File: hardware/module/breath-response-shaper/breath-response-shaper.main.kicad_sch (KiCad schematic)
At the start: 12 parts

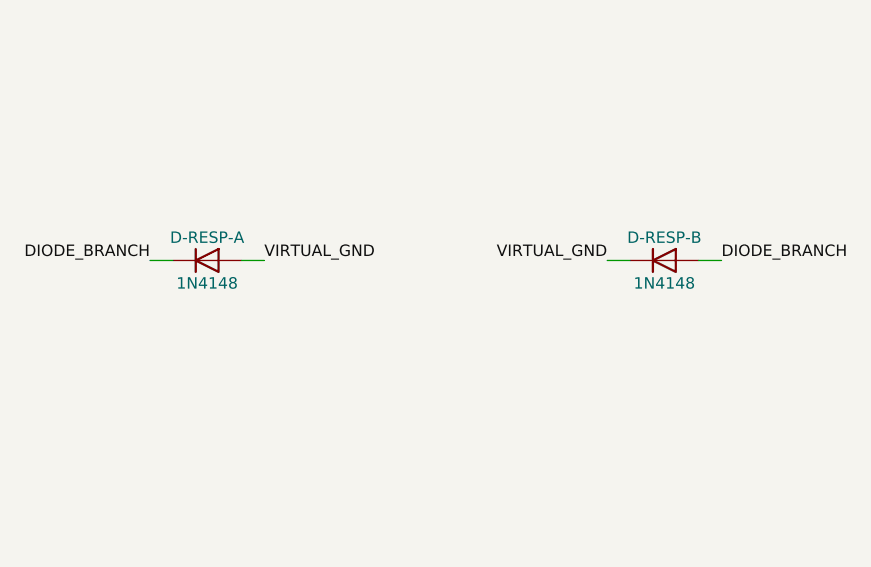
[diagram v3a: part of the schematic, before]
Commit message: Breath chain fixes (pre-layout review A1): OFFSET clockwise-positive, 1N4448W, chain sim, stale derived statements
POT-OFFSET's ends swapped on the sheet so the panel's + is true (A1-4).
D-RESP bought as Vishay 1N4448W-E3-08, datasheet banked (A1-3, owner).
Shaper-into-output-stage sim added; breath-chain-curve-clip registered (A1-1).
Working point cited as disputed (A1-6, A8-4); REF band, ADR 0006 standing
level, C_cm in the pole, R1b dispute, -12 V row, buffered label, ADC
injection current corrected (A1-8..A1-15). Sims re-run pending.

Co-Authored-By: Claude Opus 5.5 <noreply@anthropic.com>
Claude-Session: https://claude.ai/code/session_01LmB4muFXnoLprWX4JzuJ5A
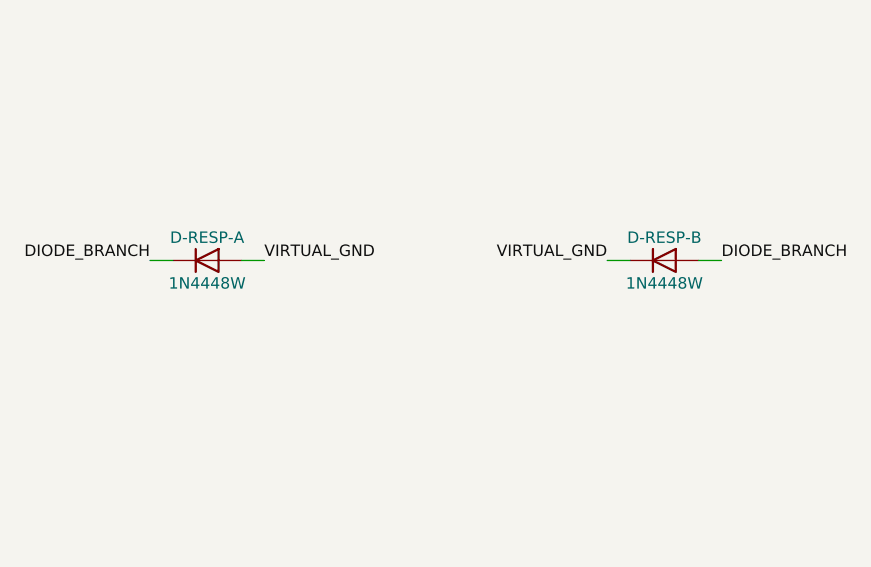
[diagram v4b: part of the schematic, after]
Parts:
- D-RESP-A, D-RESP-B: value 1N4148 -> 1N4448W; LCSC C241939 -> C3313020; MPN 1N4148W-E3-08 -> 1N4448W-E3-08; Pins_source SOD-123, cathode band; KiCad pin 1 cathode [ds datasheets/discrete-and-power/1N4148W.pdf] -> SOD-123, cathode band; KiCad pin 1 cathode [ds datasheets/discrete-and-power/1N4448W.pdf p.1, Vishay 86362, the same case and outline as its 1N4148W sibling]
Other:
- title: Response control (PROPOSED) - the module main board's page (hardware/module/breath-response-shaper) -> Response control - the module main board's page (hardware/module/breath-response-shaper)
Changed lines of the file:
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@@
   (paper "A2")
   (title_block
-    (title "Response control (PROPOSED) - the module main board's page (hardware/module/breath-response-shaper)")
-    (comment 7 "title: Response control (PROPOSED)")
+    (title "Response control - the module main board's page (hardware/module/breath-response-shaper)")
+    (comment 7 "title: Response control")
     (date "")
     (rev "")
@@
     (in_bom yes) (on_board yes) (dnp no)
     (property "Reference" "D-RESP-A" (at 396.24 185.42 0) (effects (font (size 1.27 1.27))))
-    (property "Value" "1N4148" (at 396.24 190.5 0) (effects (font (size 1.27 1.27))))
+    (property "Value" "1N4448W" (at 396.24 190.5 0) (effects (font (size 1.27 1.27))))
     (property "Footprint" "Diode_SMD:D_SOD-123" (at 396.24 193.04 0) (effects (font (size 1.27 1.27)) hide))
     (property "Datasheet" "" (at 396.24 187.96 0) (effects (font (size 1.27 1.27)) hide))
@@
     (property "Pins" "A=2(A) K=1(K)" (at 396.24 187.96 0) (effects (font (size 1.27 1.27)) hide))
     (property "Note" "One of an ANTIPARALLEL pair. Breath is unipolar so only one ever conducts in play; the other is for power-on and fault excursions" (at 396.24 187.96 0) (effects (font (size 1.27 1.27)) hide))
-    (property "Pins_source" "SOD-123, cathode band; KiCad pin 1 cathode [ds datasheets/discrete-and-power/1N4148W.pdf]" (at 396.24 187.96 0) (effects (font (size 1.27 1.27)) hide))
+    (property "Pins_source" "SOD-123, cathode band; KiCad pin 1 cathode [ds datasheets/discrete-and-power/1N4448W.pdf p.1, Vishay 86362, the same case and outline as its 1N4148W sibling]" (at 396.24 187.96 0) (effects (font (size 1.27 1.27)) hide))
     (property "Manufacturer" "Vishay" (at 396.24 187.96 0) (effects (font (size 1.27 1.27)) hide))
-    (property "MPN" "1N4148W-E3-08" (at 396.24 187.96 0) (effects (font (size 1.27 1.27)) hide))
-    (property "LCSC" "C241939" (at 396.24 187.96 0) (effects (font (size 1.27 1.27)) hide))
+    (property "MPN" "1N4448W-E3-08" (at 396.24 187.96 0) (effects (font (size 1.27 1.27)) hide))
+    (property "LCSC" "C3313020" (at 396.24 187.96 0) (effects (font (size 1.27 1.27)) hide))
     (property "Assembly" "machine" (at 396.24 187.96 0) (effects (font (size 1.27 1.27)) hide))
     (pin "1")
@@
     (in_bom yes) (on_board yes) (dnp no)
     (property "Reference" "D-RESP-B" (at 447.04 185.42 0) (effects (font (size 1.27 1.27))))
-    (property "Value" "1N4148" (at 447.04 190.5 0) (effects (font (size 1.27 1.27))))
+    (property "Value" "1N4448W" (at 447.04 190.5 0) (effects (font (size 1.27 1.27))))
     (property "Footprint" "Diode_SMD:D_SOD-123" (at 447.04 193.04 0) (effects (font (size 1.27 1.27)) hide))
     (property "Datasheet" "" (at 447.04 187.96 0) (effects (font (size 1.27 1.27)) hide))
     (property "Row" "D-RESP" (at 447.04 187.96 0) (effects (font (size 1.27 1.27)) hide))
     (property "Pins" "A=2(A) K=1(K)" (at 447.04 187.96 0) (effects (font (size 1.27 1.27)) hide))
-    (property "Pins_source" "SOD-123, cathode band; KiCad pin 1 cathode [ds datasheets/discrete-and-power/1N4148W.pdf]" (at 447.04 187.96 0) (effects (font (size 1.27 1.27)) hide))
+    (property "Pins_source" "SOD-123, cathode band; KiCad pin 1 cathode [ds datasheets/discrete-and-power/1N4448W.pdf p.1, Vishay 86362, the same case and outline as its 1N4148W sibling]" (at 447.04 187.96 0) (effects (font (size 1.27 1.27)) hide))
     (property "Manufacturer" "Vishay" (at 447.04 187.96 0) (effects (font (size 1.27 1.27)) hide))
-    (property "MPN" "1N4148W-E3-08" (at 447.04 187.96 0) (effects (font (size 1.27 1.27)) hide))
-    (property "LCSC" "C241939" (at 447.04 187.96 0) (effects (font (size 1.27 1.27)) hide))
+    (property "MPN" "1N4448W-E3-08" (at 447.04 187.96 0) (effects (font (size 1.27 1.27)) hide))
+    (property "LCSC" "C3313020" (at 447.04 187.96 0) (effects (font (size 1.27 1.27)) hide))
     (property "Assembly" "machine" (at 447.04 187.96 0) (effects (font (size 1.27 1.27)) hide))
     (pin "1")

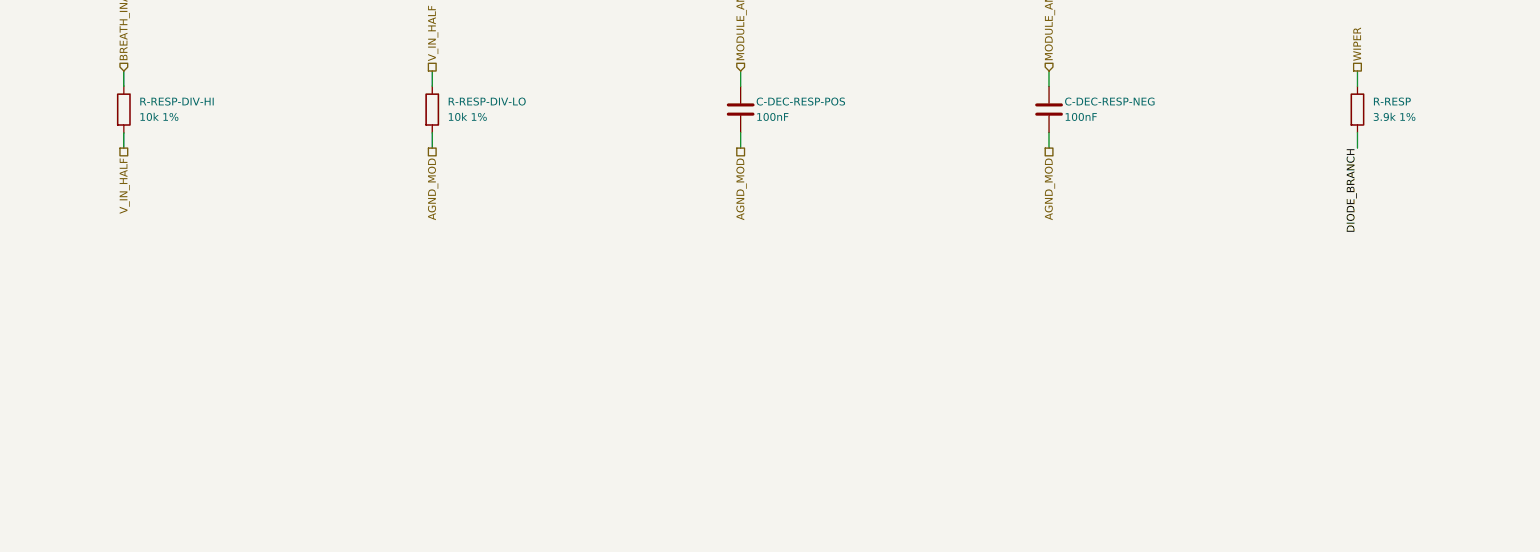
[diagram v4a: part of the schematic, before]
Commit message: Response shaper: TRIM-RESP (Bourns 3224W 10k) in series with R-RESP, now 2.7k (A1-3)
Sheet, export, renders and BOM fragment. Page, sims and figures follow.

Co-Authored-By: Claude Opus 5.5 <noreply@anthropic.com>
Claude-Session: https://claude.ai/code/session_01LmB4muFXnoLprWX4JzuJ5A
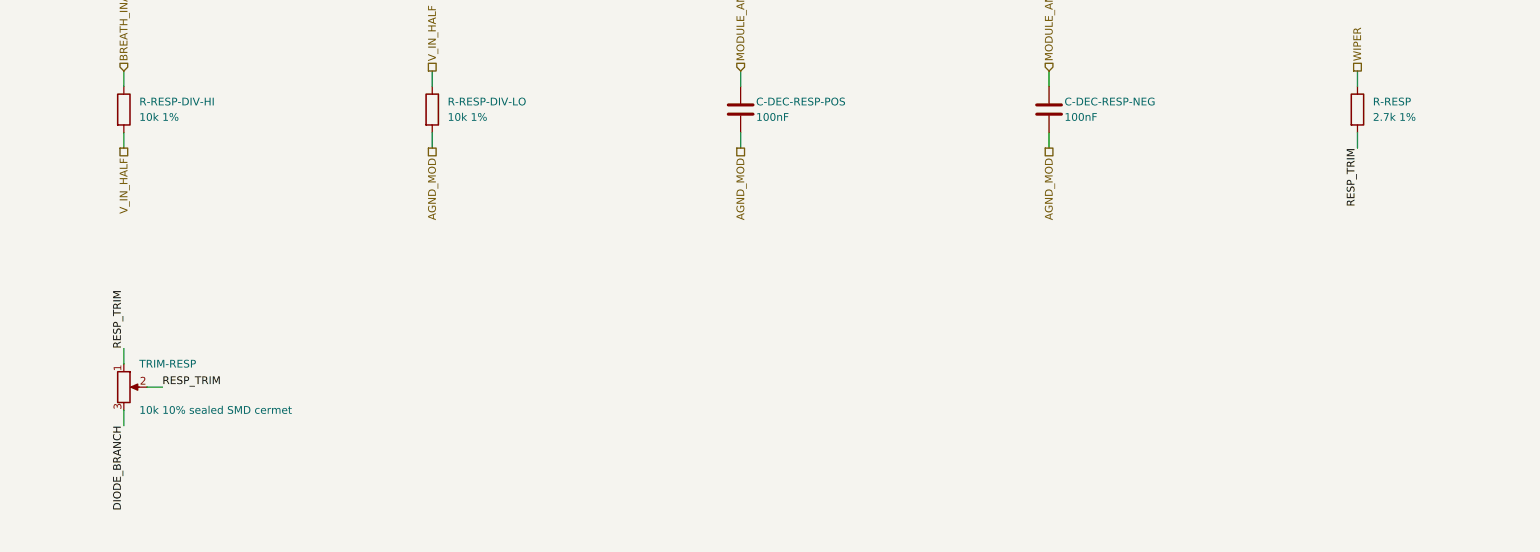
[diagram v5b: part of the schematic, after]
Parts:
- added TRIM-RESP: 10k 10% sealed SMD cermet, Potentiometer_SMD:Potentiometer_Bourns_3224W_Vertical, symbol Device:R_Potentiometer
- R-RESP: value 3.9k 1% -> 2.7k 1%; LCSC C17614 -> C17530; MPN 0805W8F3901T5E -> 0805W8F2701T5E; Note Sets how hard the curve bends: shaper-exp-gain, at least 1.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 -> The fixed part of the diode branch, in series with TRIM-RES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
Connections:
- net DIODE_BRANCH: now also TRIM-RESP.3; no longer R-RESP.2
- new net RESP_TRIM: R-RESP.2, TRIM-RESP.1, TRIM-RESP.2
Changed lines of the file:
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@@
     (in_bom yes) (on_board yes) (dnp no)
     (property "Reference" "R-RESP" (at 347.98 186.69 0) (effects (font (size 1.27 1.27)) (justify left)))
-    (property "Value" "3.9k 1%" (at 347.98 189.23 0) (effects (font (size 1.27 1.27)) (justify left)))
+    (property "Value" "2.7k 1%" (at 347.98 189.23 0) (effects (font (size 1.27 1.27)) (justify left)))
     (property "Footprint" "Resistor_SMD:R_0805_2012Metric" (at 344.17 187.96 0) (effects (font (size 1.27 1.27)) hide))
     (property "Datasheet" "" (at 345.44 187.96 0) (effects (font (size 1.27 1.27)) hide))
     (property "Row" "R-RESP" (at 345.44 187.96 0) (effects (font (size 1.27 1.27)) hide))
     (property "Pins" "1=1 2=2" (at 345.44 187.96 0) (effects (font (size 1.27 1.27)) hide))
-    (property "Note" "Sets how hard the curve bends: shaper-exp-gain, at least 1.5x at a hard blow at POT-RESP's CW end at every simulated corner (owner, 2026-09-30: 1.5x). module/breath-response-shaper/sim" (at 345.44 187.96 0) (effects (font (size 1.27 1.27)) hide))
+    (property "Note" "The fixed part of the diode branch, in series with TRIM-RESP: the trimmer's clockwise end, where the exp end bends hardest. Low enough that every simulated corner can be trimmed UP to shaper-exp-gain's target, high enough that BREATH_SHAPED still clips past 1.3x a hard blow there. module/breath-response-shaper/sim" (at 345.44 187.96 0) (effects (font (size 1.27 1.27)) hide))
     (property "Manufacturer" "UNI-ROYAL(Uniroyal Elec)" (at 345.44 187.96 0) (effects (font (size 1.27 1.27)) hide))
-    (property "MPN" "0805W8F3901T5E" (at 345.44 187.96 0) (effects (font (size 1.27 1.27)) hide))
-    (property "LCSC" "C17614" (at 345.44 187.96 0) (effects (font (size 1.27 1.27)) hide))
+    (property "MPN" "0805W8F2701T5E" (at 345.44 187.96 0) (effects (font (size 1.27 1.27)) hide))
+    (property "LCSC" "C17530" (at 345.44 187.96 0) (effects (font (size 1.27 1.27)) hide))
     (property "Assembly" "machine" (at 345.44 187.96 0) (effects (font (size 1.27 1.27)) hide))
     (pin "1")
@@
     (property "Dir" "ref" (at 345.44 181.61 0) (effects (font (size 1.27 1.27)) hide)))
   (wire (pts (xy 345.44 191.77) (xy 345.44 194.31)) (stroke (width 0) (type default)))
-  (label "DIODE_BRANCH" (at 345.44 194.31 270) (fields_autoplaced) (effects (font (size 1.27 1.27)) (justify right bottom)))
+  (label "RESP_TRIM" (at 345.44 194.31 270) (fields_autoplaced) (effects (font (size 1.27 1.27)) (justify right bottom)))
   (wire (pts (xy 392.43 187.96) (xy 389.89 187.96)) (stroke (width 0) (type default)))
   (label "DIODE_BRANCH" (at 389.89 187.96 180) (fields_autoplaced) (effects (font (size 1.27 1.27)) (justify right bottom)))
@@
     (property "Dir" "out" (at 91.44 240.03 0) (effects (font (size 1.27 1.27)) hide))
     (property "To" "module/breath-output-stage" (at 91.44 240.03 0) (effects (font (size 1.27 1.27)) hide)))
+  (symbol (lib_id "Device:R_Potentiometer") (at 142.24 233.68 0) (unit 1)
+    (in_bom yes) (on_board yes) (dnp no)
+    (property "Reference" "TRIM-RESP" (at 144.78 229.87 0) (effects (font (size 1.27 1.27)) (justify left)))
+    (property "Value" "10k 10% sealed SMD cermet" (at 144.78 237.49 0) (effects (font (size 1.27 1.27)) (justify left)))
+    (property "Footprint" "Potentiometer_SMD:Potentiometer_Bourns_3224W_Vertical" (at 142.24 233.68 0) (effects (font (size 1.27 1.27)) hide))
+    (property "Datasheet" "" (at 142.24 233.68 0) (effects (font (size 1.27 1.27)) hide))
+    (property "Row" "TRIM-RESP" (at 142.24 233.68 0) (effects (font (size 1.27 1.27)) hide))
+    (property "Pins" "CW=3(3) W=2(2) CCW=1(1)" (at 142.24 233.68 0) (effects (font (size 1.27 1.27)) hide))
+    (property "Note" "IN SERIES with R-RESP, its wiper strapped to its CCW end, so clockwise LOWERS the branch's resistance and RAISES the exp end's gain - the panel knob's sense. An open wiper leaves the whole track in series: LESS gain, never more. Set once at commissioning (E10) to shaper-exp-gain's trimmed target at a hard blow, POT-RESP fully CW. module/breath-response-shaper/sim" (at 142.24 233.68 0) (effects (font (size 1.27 1.27)) hide))
+    (property "Pins_source" "datasheets/discrete-and-power/BOURNS-3224-TRIMPOT.pdf p.1 schematic: 1 CCW, 2 wiper, 3 CW" (at 142.24 233.68 0) (effects (font (size 1.27 1.27)) hide))
+    (property "Manufacturer" "Bourns" (at 142.24 233.68 0) (effects (font (size 1.27 1.27)) hide))
+    (property "MPN" "3224W-1-103E" (at 142.24 233.68 0) (effects (font (size 1.27 1.27)) hide))
+    (property "LCSC" "C81348" (at 142.24 233.68 0) (effects (font (size 1.27 1.27)) hide))
+    (property "Assembly" "hand" (at 142.24 233.68 0) (effects (font (size 1.27 1.27)) hide))
+    (pin "1")
+    (pin "2")
+    (pin "3")
+    (instances (project "module-main" (path "/fc77e9f9-9171-5c83-92ae-8cafe880764e/c482d433-655e-5e81-83d2-2324ffc55f2a" (reference "RV4") (unit 1))) (project "breath-response-shaper.main" (path "/b720220a-6b4f-50eb-8ff6-c33665ae6827" (reference "TRIM-RESP") (unit 1))) (project "breath-response-shaper" (path "/97139bb3-9c58-5159-a2a9-3813e79c635b/c16928c3-e665-533e-bb80-5b6da545f796" (reference "TRIM-RESP") (unit 1))))
+  )
+  (wire (pts (xy 142.24 229.87) (xy 142.24 227.33)) (stroke (width 0) (type default)))
+  (label "RESP_TRIM" (at 142.24 227.33 90) (fields_autoplaced) (effects (font (size 1.27 1.27)) (justify left bottom)))
+  (wire (pts (xy 146.05 233.68) (xy 148.59 233.68)) (stroke (width 0) (type default)))
+  (label "RESP_TRIM" (at 148.59 233.68 0) (fields_autoplaced) (effects (font (size 1.27 1.27)) (justify left bottom)))
+  (wire (pts (xy 142.24 237.49) (xy 142.24 240.03)) (stroke (width 0) (type default)))
+  (label "DIODE_BRANCH" (at 142.24 240.03 270) (fields_autoplaced) (effects (font (size 1.27 1.27)) (justify right bottom)))
   (sheet_instances (path "/" (page "1")))
 )
